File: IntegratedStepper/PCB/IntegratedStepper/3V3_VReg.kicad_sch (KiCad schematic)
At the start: 0 parts

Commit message: update Vreg for Integrated Stepper
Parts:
- added C3 (x3): 10uf, Capacitor_SMD:C_0603_1608Metric_Pad1.08x0.95mm_HandSolder, symbol SamacSys_Parts:0402B102K500NT
- added C3 (x2): 1uF, Capacitor_SMD:C_0603_1608Metric_Pad1.08x0.95mm_HandSolder, symbol SamacSys_Parts:0402B102K500NT
- added C4: 0.1uF, Capacitor_SMD:C_0603_1608Metric_Pad1.08x0.95mm_HandSolder, symbol SamacSys_Parts:0402B102K500NT
- added C4 (x2): 100nf, Capacitor_SMD:C_0603_1608Metric_Pad1.08x0.95mm_HandSolder, symbol SamacSys_Parts:0402B102K500NT
- added D1, D2: PMEG6020ER,115, PMEG6020ER115, symbol SamacSys_Parts:PMEG6020ER,115
- added IC3: LMR38020FSQDDARQ1, SOIC127P600X170-9N, symbol SamacSys_Parts:LMR38020FSQDDARQ1
- added L1: 10uH, SamacSys_Parts:INDPM6965X300N, symbol SamacSys_Parts:IHLP2525CZER100M01
- added R5 (x2): 154k, RESC1608X55N, symbol SamacSys_Parts:RMCF0603ZT0R00
- added R5 (x2): 64.9k, RESC1608X55N, symbol SamacSys_Parts:RMCF0603ZT0R00
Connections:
- new net: IC3.5 (FB), R5.1, R5.2
- new net: C4.1, IC3.7 (BOOT)
- new net: C4.2, IC3.8 (SW), L1.1
- new net: IC3.6 (PG), R5.1
- new net: IC3.4 (RT/SYNC), R5.1
- new net 3V3_VCC: C3.1, C3.1, C3.1, C4.1, L1.2, R5.1
- new net GND: IC3.1 (GND)
- new net VIN: C3.2, C3.2, C4.2, D1.1 (K), D2.1 (K), IC3.2 (EN), IC3.3 (VIN)
- new net VM: D1.2 (A)
- new net VS: C3.1, C3.1, C3.2, C3.2, C3.2, C4.1, C4.2, IC3.9 (EP), R5.2, R5.2, R5.2
- new net V_USB: D2.2 (A)

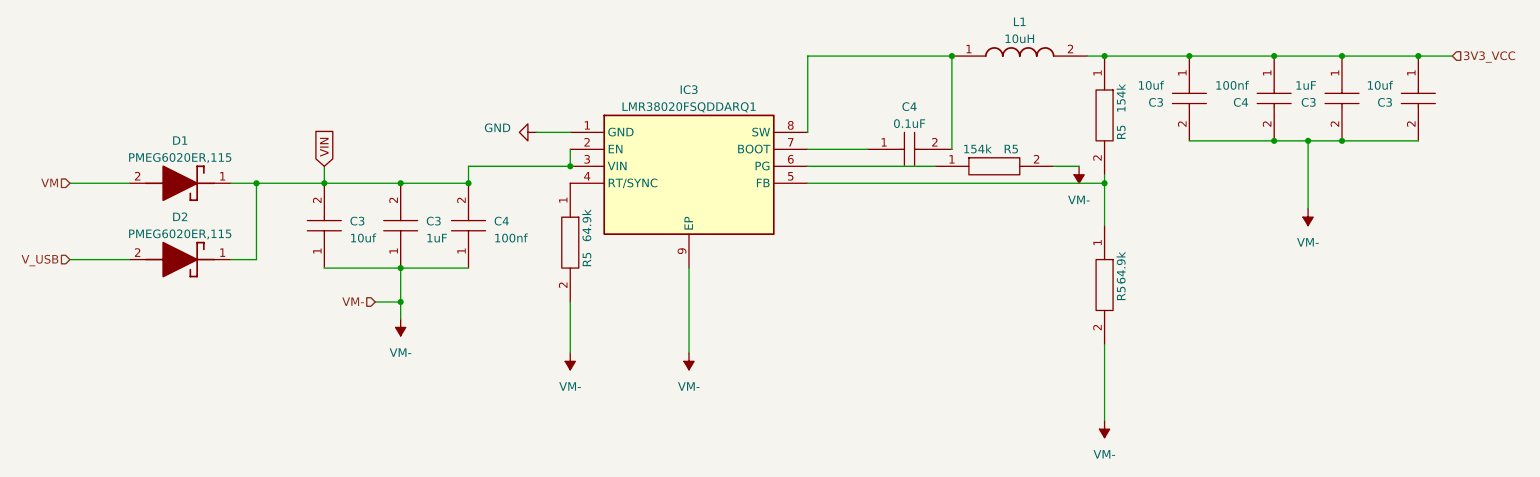
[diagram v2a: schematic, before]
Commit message: Update Integrated Stepper PCB with ESP sch and CAN sch
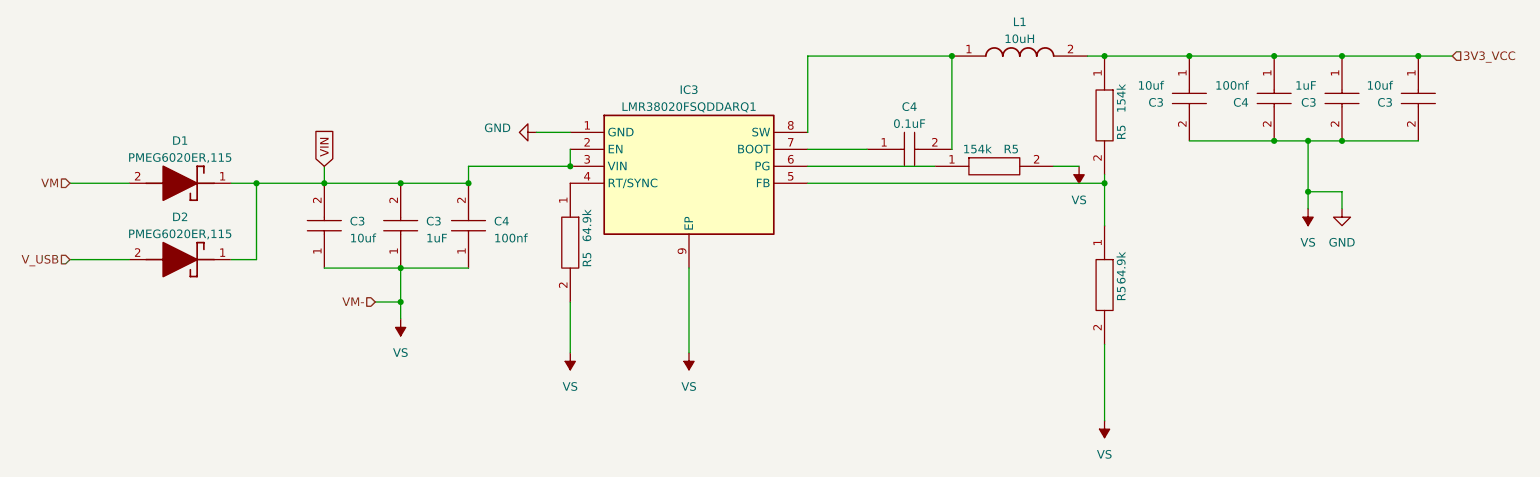
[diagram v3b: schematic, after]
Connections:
- net VS is gone; now on net GND: C3.1, C3.1, C3.2, C3.2, C3.2, C4.1, C4.2, IC3.9 (EP), R5.2, R5.2, R5.2

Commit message: Update Integrated Stepper with inital PCB
This is going to be so hard :(
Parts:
- D1, D2: footprint PMEG6020ER115 -> SamacSys_Parts:PMEG6020ER115
- IC3: footprint SOIC127P600X170-9N -> SamacSys_Parts:SOIC127P600X170-9N
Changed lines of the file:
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@@
 			)
 		)
-		(property "Footprint" "PMEG6020ER115"
+		(property "Footprint" "SamacSys_Parts:PMEG6020ER115"
 			(at 52.07 5.41 0)
 			(effects
@@
 			)
 		)
-		(property "Footprint" "PMEG6020ER115"
+		(property "Footprint" "SamacSys_Parts:PMEG6020ER115"
 			(at 52.07 16.84 0)
 			(effects
@@
 			)
 		)
-		(property "Footprint" "SOIC127P600X170-9N"
+		(property "Footprint" "SamacSys_Parts:SOIC127P600X170-9N"
 			(at 144.78 186.36 0)
 			(effects

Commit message: add changes for instock parts
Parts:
- D1, D2: LCSC (none) -> C98663; LCSC Part (none) -> C98663; LCSC Part Number (none) -> C98663
- IC3: LCSC (none) -> C5149193; LCSC Part (none) -> C5149193; LCSC Part Number (none) -> C5149193
- L1: footprint SamacSys_Parts:INDPM6965X300N -> easyeda2kicad:IND-SMD_L7.2-W6.6_GPSR07X0; LCSC (none) -> C5189959; LCSC Part (none) -> C5189959; LCSC Part Number (none) -> C5189959
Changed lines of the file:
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@@
+			)
+		)
+		(property "LCSC" "C98663"
+			(at 64.77 99.06 0)
+			(effects
+				(font
+					(size 1.27 1.27)
+				)
+				(hide yes)
+			)
+		)
+		(property "LCSC Part" "C98663"
+			(at 64.77 99.06 0)
+			(effects
+				(font
+					(size 1.27 1.27)
+				)
+				(hide yes)
+			)
+		)
+		(property "LCSC Part Number" "C98663"
+			(at 64.77 99.06 0)
+			(effects
+				(font
+					(size 1.27 1.27)
+				)
+				(hide yes)
 			)
 		)
@@
 			)
 		)
-		(property "Footprint" "SamacSys_Parts:INDPM6965X300N"
+		(property "Footprint" "easyeda2kicad:IND-SMD_L7.2-W6.6_GPSR07X0"
 			(at 186.69 176.2 0)
 			(effects
@@
 				)
 				(justify left top)
+				(hide yes)
+			)
+		)
+		(property "LCSC" "C5189959"
+			(at 170.18 80.01 0)
+			(effects
+				(font
+					(size 1.27 1.27)
+				)
+				(hide yes)
+			)
+		)
+		(property "LCSC Part" "C5189959"
+			(at 170.18 80.01 0)
+			(effects
+				(font
+					(size 1.27 1.27)
+				)
+				(hide yes)
+			)
+		)
+		(property "LCSC Part Number" "C5189959"
+			(at 170.18 80.01 0)
+			(effects
+				(font
+					(size 1.27 1.27)
+				)
 				(hide yes)
 			)
@@
 			)
 		)
+		(property "LCSC" "C98663"
+			(at 64.77 110.49 0)
+			(effects
+				(font
+					(size 1.27 1.27)
+				)
+				(hide yes)
+			)
+		)
+		(property "LCSC Part" "C98663"
+			(at 64.77 110.49 0)
+			(effects
+				(font
+					(size 1.27 1.27)
+				)
+				(hide yes)
+			)
+		)
+		(property "LCSC Part Number" "C98663"
+			(at 64.77 110.49 0)
+			(effects
+				(font
+					(size 1.27 1.27)
+				)
+				(hide yes)
+			)
+		)
 		(pin "1"
 		)
@@
 				(hide yes)
 			)
+		)
+		(property "LCSC" "C5149193"
+			(at 113.03 91.44 0)
+			(effects
+				(font
+					(size 1.27 1.27)
+				)
+				(hide yes)
+			)
+		)
+		(property "LCSC Part" "C5149193"
+			(at 113.03 91.44 0)
+			(effects
+				(font
+					(size 1.27 1.27)
+				)
+				(hide yes)
+			)
+		)
+		(property "LCSC Part Number" "C5149193"
+			(at 113.03 91.44 0)
+			(effects
+				(font
+					(size 1.27 1.27)
+				)
+				(hide yes)
+			)

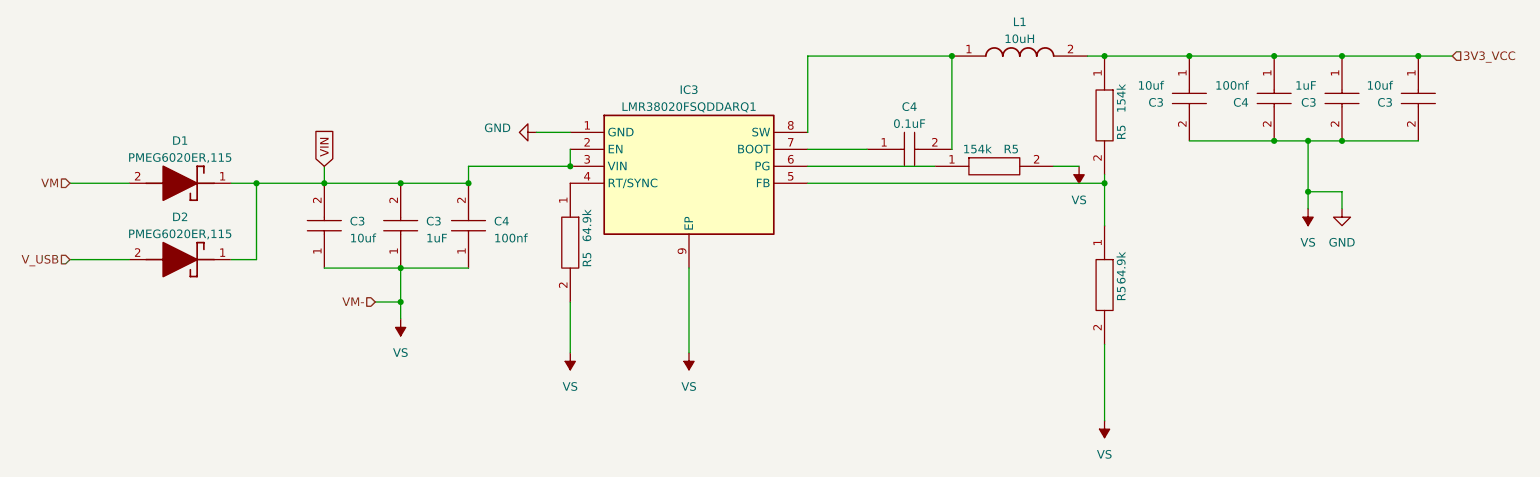
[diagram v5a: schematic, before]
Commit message: update with more in stock parts
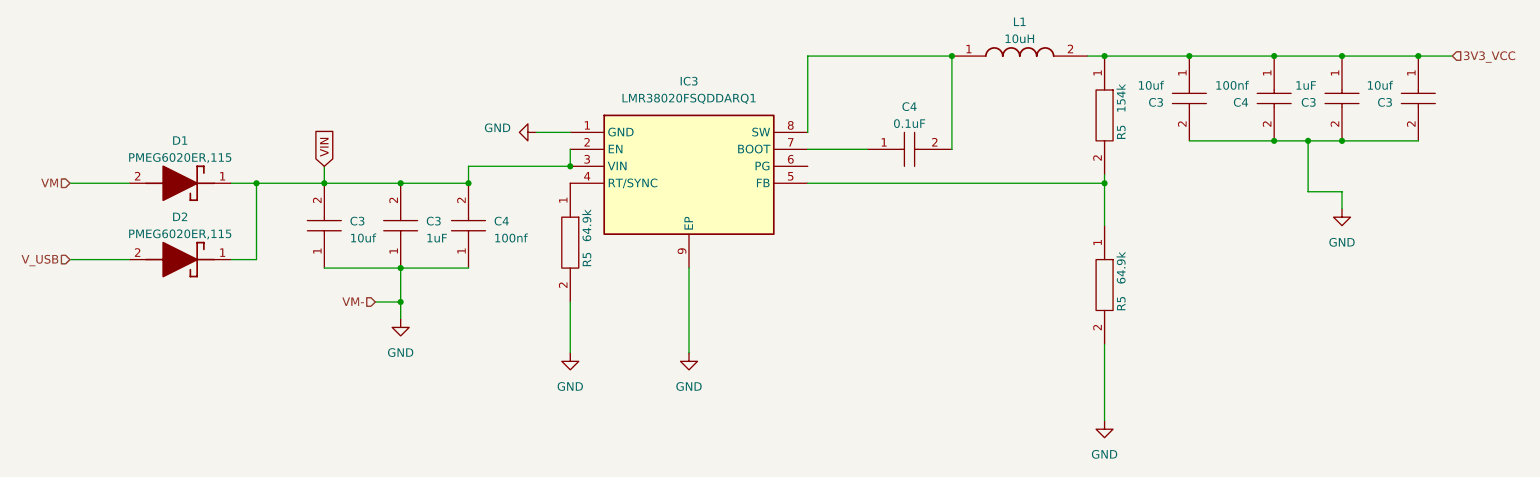
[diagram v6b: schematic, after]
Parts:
- removed R5: 154k, RESC1608X55N, symbol SamacSys_Parts:RMCF0603ZT0R00
- C3: LCSC (none) -> C96446; LCSC Part (none) -> C96446
- C3: LCSC (none) -> C15849; LCSC Part (none) -> C15849; LCSC Part Number C15849 -> C15849
- C4: LCSC (none) -> C14663; LCSC Part (none) -> C14663
- R5: footprint RESC1608X55N -> Resistor_SMD:R_0603_1608Metric; LCSC (none) -> C425661; LCSC Part (none) -> C425661; LCSC Part Number C3016414 -> C425661
- R5: footprint RESC1608X55N -> Resistor_SMD:R_0603_1608Metric; LCSC (none) -> C912530; LCSC Part (none) -> C912530; LCSC Part Number C3016414 -> C912530
- R5: footprint RESC1608X55N -> Resistor_SMD:R_0603_1608Metric; LCSC (none) -> C912530; LCSC Part (none) -> C912530; LCSC Part Number C101235 -> C912530
